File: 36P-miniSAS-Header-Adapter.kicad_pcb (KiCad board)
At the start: 2 copper layers, 28.8 x 50 mm, 4 parts, among them J1 1888863-4, J2 Conn_02x18

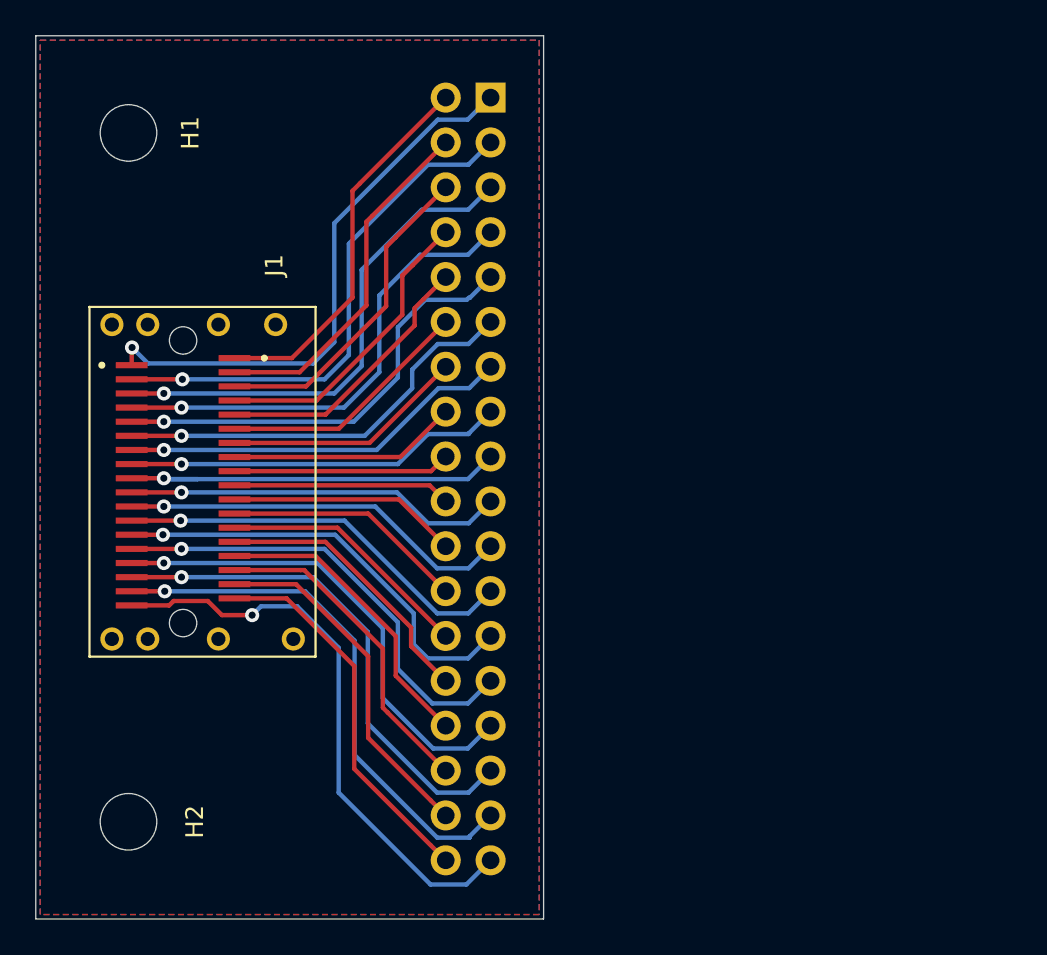
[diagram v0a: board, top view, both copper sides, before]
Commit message: Finalize pcb routing
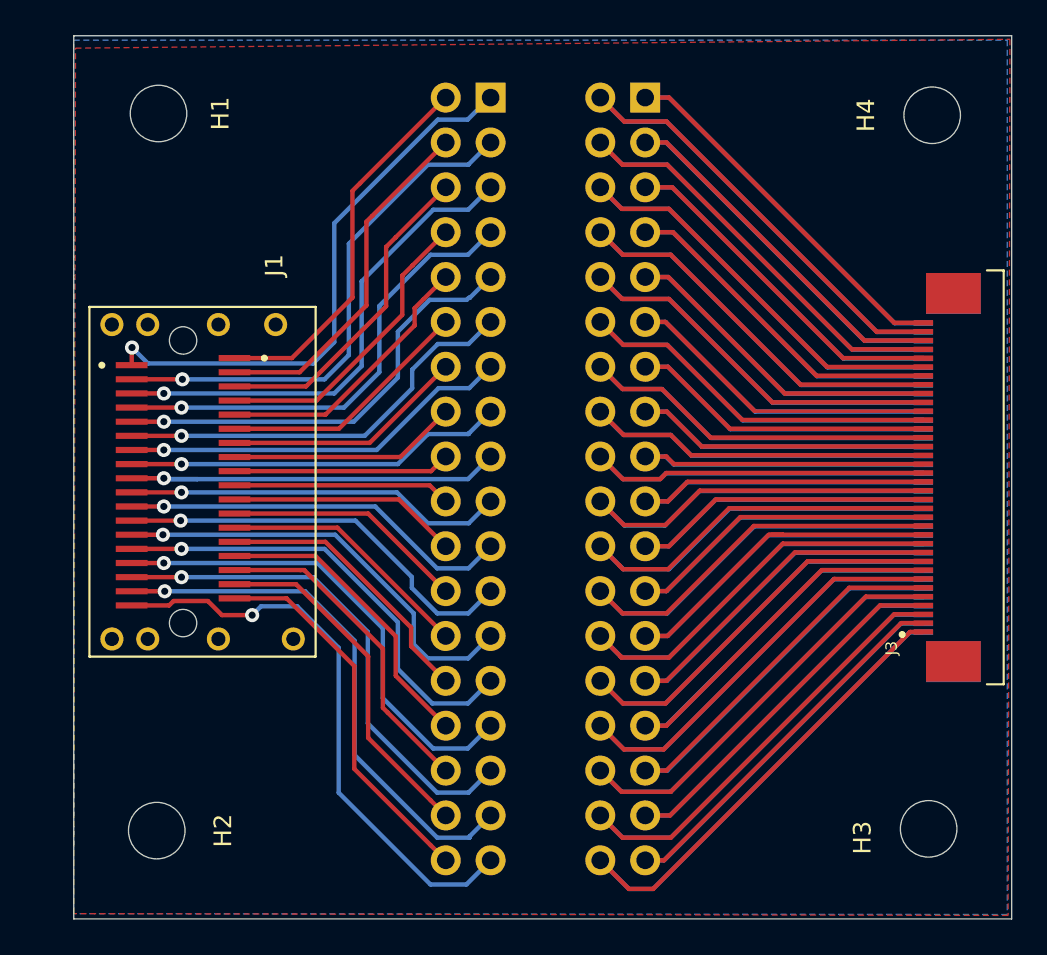
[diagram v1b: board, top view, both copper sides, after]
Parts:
- added H3: MountingHole, MountingHole:MountingHole_3.2mm_M3, F.Cu at (197.8, 22.4)
- added H4: MountingHole, MountingHole:MountingHole_3.2mm_M3, F.Cu at (198.0, -18.0)
- added J3: 3-1734592-6, footprints:TE_3-1734592-6, F.Cu at (197.5, 2.50)
- added J4: Header_02x18, Connector_PinHeader_2.54mm:PinHeader_2x18_P2.54mm_Vertical, B.Cu at (181.8, -19.0)
- added J5: 3-1734592-6, footprints:TE_3-1734592-6, B.Cu at (197.5, 2.52)
- J2: value Conn_02x18 -> Header_02x18
- moved H1 2.02 mm to (154.2, -18.1)
- moved H2 1.68 mm to (154.1, 22.5)
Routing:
- net /36: track 0.00 -> 50.0 mm
- net /34: track 0.00 -> 48.1 mm
- net /2: track 0.00 -> 47.6 mm
- net /32: track 0.00 -> 46.7 mm
- net /4: track 0.00 -> 46.3 mm
- net /30: track 0.00 -> 45.7 mm
- net /6: track 0.00 -> 45.0 mm
- net /28: track 0.00 -> 44.3 mm
- net /8: track 0.00 -> 43.7 mm
- net /26: track 0.00 -> 43.0 mm
- net /35: track 0.00 -> 42.6 mm
- net /10: track 0.00 -> 42.5 mm
- net /1: track 0.00 -> 42.1 mm
- net /24: track 0.00 -> 41.7 mm
- net /33: track 0.00 -> 41.3 mm
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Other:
- board size 28.8 x 50 mm -> 53.1 x 50 mm
- rule trace_min: 0.2 -> 0.16
